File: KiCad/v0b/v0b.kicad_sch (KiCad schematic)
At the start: 34 parts, among them U1 SST39SF040, U10 MCP1700, U2 74HC139, U3 74HC174, U4 74HC191, U5 74HC191, U6 74HC191, U7 74HC670, U8 62256, U9 SAM2695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

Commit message: v0b update
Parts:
- removed R6: 3.3KΩ, PCM_Resistor_THT_AKL:R_Axial_DIN0204_L3.6mm_D1.6mm_P2.54mm_Vertical, symbol Device:R_Small
- removed RN1: R_Network03, Resistor_THT:R_Array_SIP4, symbol Device:R_Network03
- added C17: 1nF, Capacitor_THT:C_Disc_D3.0mm_W1.6mm_P2.50mm, symbol Device:C_Small
- added D1: 1N4148, Diode_THT:D_DO-34_SOD68_P2.54mm_Vertical_AnodeUp, symbol Diode:1N4148
- added R4: 4.7K, PCM_Resistor_THT_AKL:R_Axial_DIN0204_L3.6mm_D1.6mm_P2.54mm_Vertical, symbol Device:R_Small
- added RN1: R_Network04, Resistor_THT:R_Array_SIP5, symbol Device:R_Network04
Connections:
- net +3V3: no longer U9.38 (~{RST}/~{PD})
- net GND: now also R4.1
- net VCC: now also C17.2; no longer U3.1 (~{Mr})
- net pA11: now also RN1.1 (common)
- net pBank0: now also RN1.5 (R4)
- net pBank1: now also RN1.3 (R2)
- net pBank2: now also RN1.4 (R3)
- net pBank3: now also RN1.2 (R1)
- net at H1.32 (M2): now also D1.2 (A)
- new net ~{RESET}: C17.1, D1.1 (K), R4.2, U3.1 (~{Mr}), U9.38 (~{RST}/~{PD})
- no-connect marks 24 -> 23

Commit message: update v0b and README documentation
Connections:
- net cD4: no longer U3.14 (D5)
- net cD5: no longer U3.3 (D0)
- net cD6: now also U3.3 (D0)
- net cD7: now also U3.14 (D5)
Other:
- note added: ".... bbbb"
- note added: "dddd dddd"
- note added: "is.. bbbb"
- moved on the sheet: C1, C2, U10

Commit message: update v0b
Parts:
- added JP2, JP3, JP4: SolderJumper_2_Open, Jumper:SolderJumper-2_P1.3mm_Open_RoundedPad1.0x1.5mm, symbol Jumper:SolderJumper_2_Open
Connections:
- net pA11: now also JP2.1 (A)
- net pA12: now also JP3.1 (A)
- net pA13: now also JP4.1 (A)
- net pBank0: now also JP2.2 (B)
- net pBank1: now also JP3.2 (B)
- net pBank2: now also JP4.2 (B)
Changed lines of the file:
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@@
   (junction (at 81.28 124.46) (diameter 0) (color 0 0 0 0)
   )
+  (junction (at 72.39 80.645) (diameter 0) (color 0 0 0 0)
+  )
   (junction (at 68.58 190.5) (diameter 0) (color 0 0 0 0)
   )
@@
   (junction (at 21.59 163.83) (diameter 0) (color 0 0 0 0)
   )
+  (junction (at 69.85 76.2) (diameter 0) (color 0 0 0 0)
+  )
   (junction (at 246.38 157.48) (diameter 0) (color 0 0 0 0)
   )
@@
   )
   (junction (at 77.47 124.46) (diameter 0) (color 0 0 0 0)
+  )
+  (junction (at 74.93 85.09) (diameter 0) (color 0 0 0 0)
   )
   (junction (at 137.795 32.385) (diameter 0) (color 0 0 0 0)
@@
     (stroke (width 0) (type default))
   )
+  (wire (pts (xy 74.93 73.025) (xy 74.93 85.09))
+    (stroke (width 0) (type default))
+  )
   (wire (pts (xy 77.47 124.46) (xy 81.28 124.46))
     (stroke (width 0) (type default))
@@
     (stroke (width 0) (type default))
   )
+  (wire (pts (xy 72.39 80.645) (xy 72.39 87.63))
+    (stroke (width 0) (type default))
+  )
   (wire (pts (xy 117.475 59.055) (xy 111.125 59.055))
     (stroke (width 0) (type default))
@@
     (stroke (width 0) (type default))
   )
+  (wire (pts (xy 72.39 73.025) (xy 72.39 80.645))
+    (stroke (width 0) (type default))
+  )
   (wire (pts (xy 252.73 157.48) (xy 259.08 157.48))
     (stroke (width 0) (type default))
@@
     (stroke (width 0) (type default))
   )
+  (wire (pts (xy 69.85 76.2) (xy 69.85 87.63))
+    (stroke (width 0) (type default))
+  )
   (wire (pts (xy 68.58 190.5) (xy 71.12 190.5))
     (stroke (width 0) (type default))
   )
+  (wire (pts (xy 69.85 73.025) (xy 69.85 76.2))
+    (stroke (width 0) (type default))
+  )
   (wire (pts (xy 193.04 118.11) (xy 203.2 118.11))
     (stroke (width 0) (type default))
@@
   )
   (wire (pts (xy 31.75 162.56) (xy 31.75 163.83))
+    (stroke (width 0) (type default))
+  )
+  (wire (pts (xy 74.93 85.09) (xy 74.93 87.63))
     (stroke (width 0) (type default))
   )
@@
     (effects (font (size 1.27 1.27)) (justify right bottom))
   )
+  (label "pA12" (at 64.77 80.645 180) (fields_autoplaced)
+    (effects (font (size 1.27 1.27)) (justify right bottom))
+  )
   (label "cBank2" (at 36.83 87.63 90) (fields_autoplaced)
     (effects (font (size 1.27 1.27)) (justify left bottom))
@@
     (effects (font (size 1.27 1.27)) (justify left bottom))
   )
-  (label "pBank1" (at 72.39 87.63 90) (fields_autoplaced)
+  (label "pBank1" (at 72.39 73.025 90) (fields_autoplaced)
     (effects (font (size 1.27 1.27)) (justify left bottom))
   )
@@
     (effects (font (size 1.27 1.27)) (justify right bottom))
   )
+  (label "pA13" (at 67.31 85.09 180) (fields_autoplaced)
+    (effects (font (size 1.27 1.27)) (justify right bottom))
+  )
   (label "cD4" (at 137.795 118.745 180) (fields_autoplaced)
     (effects (font (size 1.27 1.27)) (justify right bottom))
@@
     (effects (font (size 1.27 1.27)) (justify right bottom))
   )
+  (label "pA11" (at 62.23 76.2 180) (fields_autoplaced)
+    (effects (font (size 1.27 1.27)) (justify right bottom))
+  )
   (label "cD0" (at 105.41 175.26 0) (fields_autoplaced)
     (effects (font (size 1.27 1.27)) (justify left bottom))
@@
     (effects (font (size 1.27 1.27)) (justify right bottom))
   )
-  (label "pBank0" (at 69.85 87.63 90) (fields_autoplaced)
+  (label "pBank0" (at 69.85 73.025 90) (fields_autoplaced)
     (effects (font (size 1.27 1.27)) (justify left bottom))
   )
@@
     (effects (font (size 1.27 1.27)) (justify right bottom))
   )
-  (label "pBank2" (at 74.93 87.63 90) (fields_autoplaced)
+  (label "pBank2" (at 74.93 73.025 90) (fields_autoplaced)
     (effects (font (size 1.27 1.27)) (justify left bottom))
   )
@@
     )
   )
+  (symbol (lib_id "Jumper:SolderJumper_2_Open") (at 71.12 85.09 0) (unit 1)
+    (in_bom yes) (on_board yes) (dnp no)
+    (property "Reference" "JP4" (at 71.12 78.74 0)
+      (effects (font (size 1.27 1.27)))
+    )
+    (property "Value" "SolderJumper_2_Open" (at 51.435 85.725 0)
+      (effects (font (size 1.27 1.27)))
+    )
+    (property "Footprint" "Jumper:SolderJumper-2_P1.3mm_Open_RoundedPad1.0x1.5mm" (at 71.12 85.09 0)
+      (effects (font (size 1.27 1.27)) hide)
+    )
+    (property "Datasheet" "~" (at 71.12 85.09 0)
+      (effects (font (size 1.27 1.27)) hide)
+    )
+    (pin "2")
+    (pin "1")
+    (instances
+      (project "v0b"
+        (path "/06c728bd-36f8-4444-b104-295b6423c2d2"
+          (reference "JP4") (unit 1)
+        )
+      )
+    )
+  )
   (symbol (lib_id "power:VCC") (at 62.23 100.33 180) (unit 1)
     (in_bom yes) (on_board yes) (dnp no)
@@
         (path "/06c728bd-36f8-4444-b104-295b6423c2d2"
           (reference "#PWR05") (unit 1)
+        )
+      )
+    )
+  )
+  (symbol (lib_id "Jumper:SolderJumper_2_Open") (at 66.04 76.2 0) (unit 1)
+    (in_bom yes) (on_board yes) (dnp no)
+    (property "Reference" "JP2" (at 66.04 69.85 0)
+      (effects (font (size 1.27 1.27)))
+    )
+    (property "Value" "SolderJumper_2_Open" (at 46.355 76.835 0)
+      (effects (font (size 1.27 1.27)))
+    )
+    (property "Footprint" "Jumper:SolderJumper-2_P1.3mm_Open_RoundedPad1.0x1.5mm" (at 66.04 76.2 0)
+      (effects (font (size 1.27 1.27)) hide)
+    )
+    (property "Datasheet" "~" (at 66.04 76.2 0)
+      (effects (font (size 1.27 1.27)) hide)
+    )
+    (pin "2")
+    (pin "1")
+    (instances
+      (project "v0b"
+        (path "/06c728bd-36f8-4444-b104-295b6423c2d2"
+          (reference "JP2") (unit 1)
         )
       )
@@
         )
       )
+    )
+  )
+  (symbol (lib_id "Jumper:SolderJumper_2_Open") (at 68.58 80.645 0) (unit 1)
+    (in_bom yes) (on_board yes) (dnp no)
+    (property "Reference" "JP3" (at 68.58 74.295 0)
+      (effects (font (size 1.27 1.27)))
+    )
+    (property "Value" "SolderJumper_2_Open" (at 48.895 81.28 0)
+      (effects (font (size 1.27 1.27)))
+    )
+    (property "Footprint" "Jumper:SolderJumper-2_P1.3mm_Open_RoundedPad1.0x1.5mm" (at 68.58 80.645 0)
+      (effects (font (size 1.27 1.27)) hide)
+    )
+    (property "Datasheet" "~" (at 68.58 80.645 0)
+      (effects (font (size 1.27 1.27)) hide)
+    )
+    (pin "2")
+    (pin "1")
+    (instances
+      (project "v0b"
+        (path "/06c728bd-36f8-4444-b104-295b6423c2d2"
+          (reference "JP3") (unit 1)
+        )
+      )

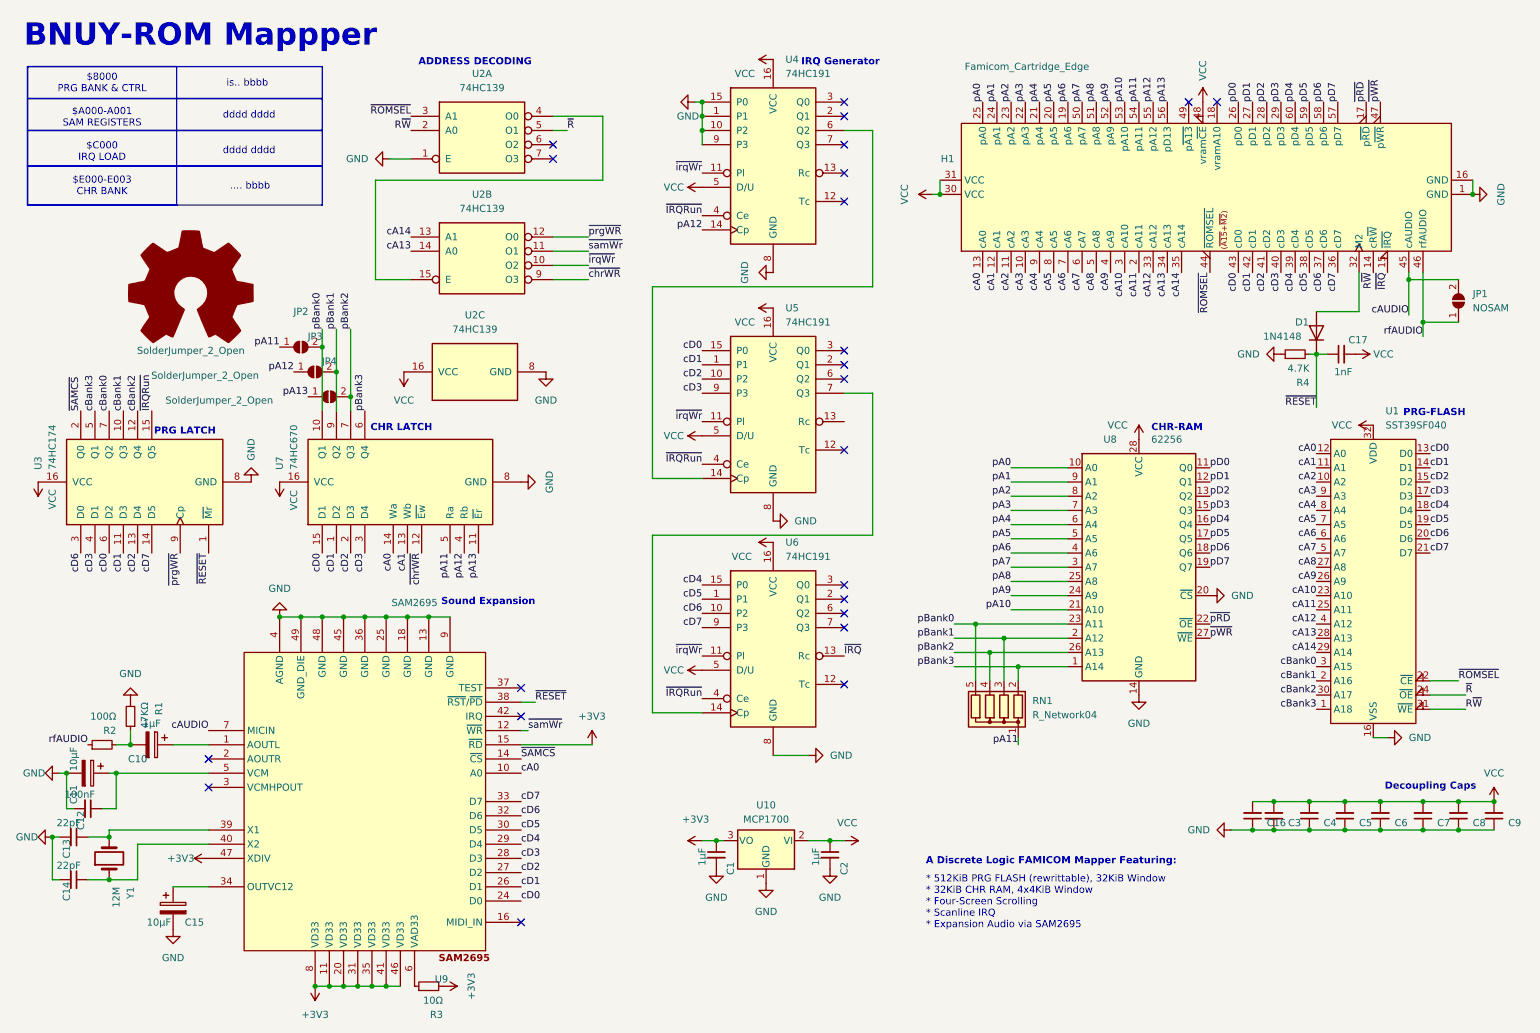
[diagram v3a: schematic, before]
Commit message: Update README, v0b schematic
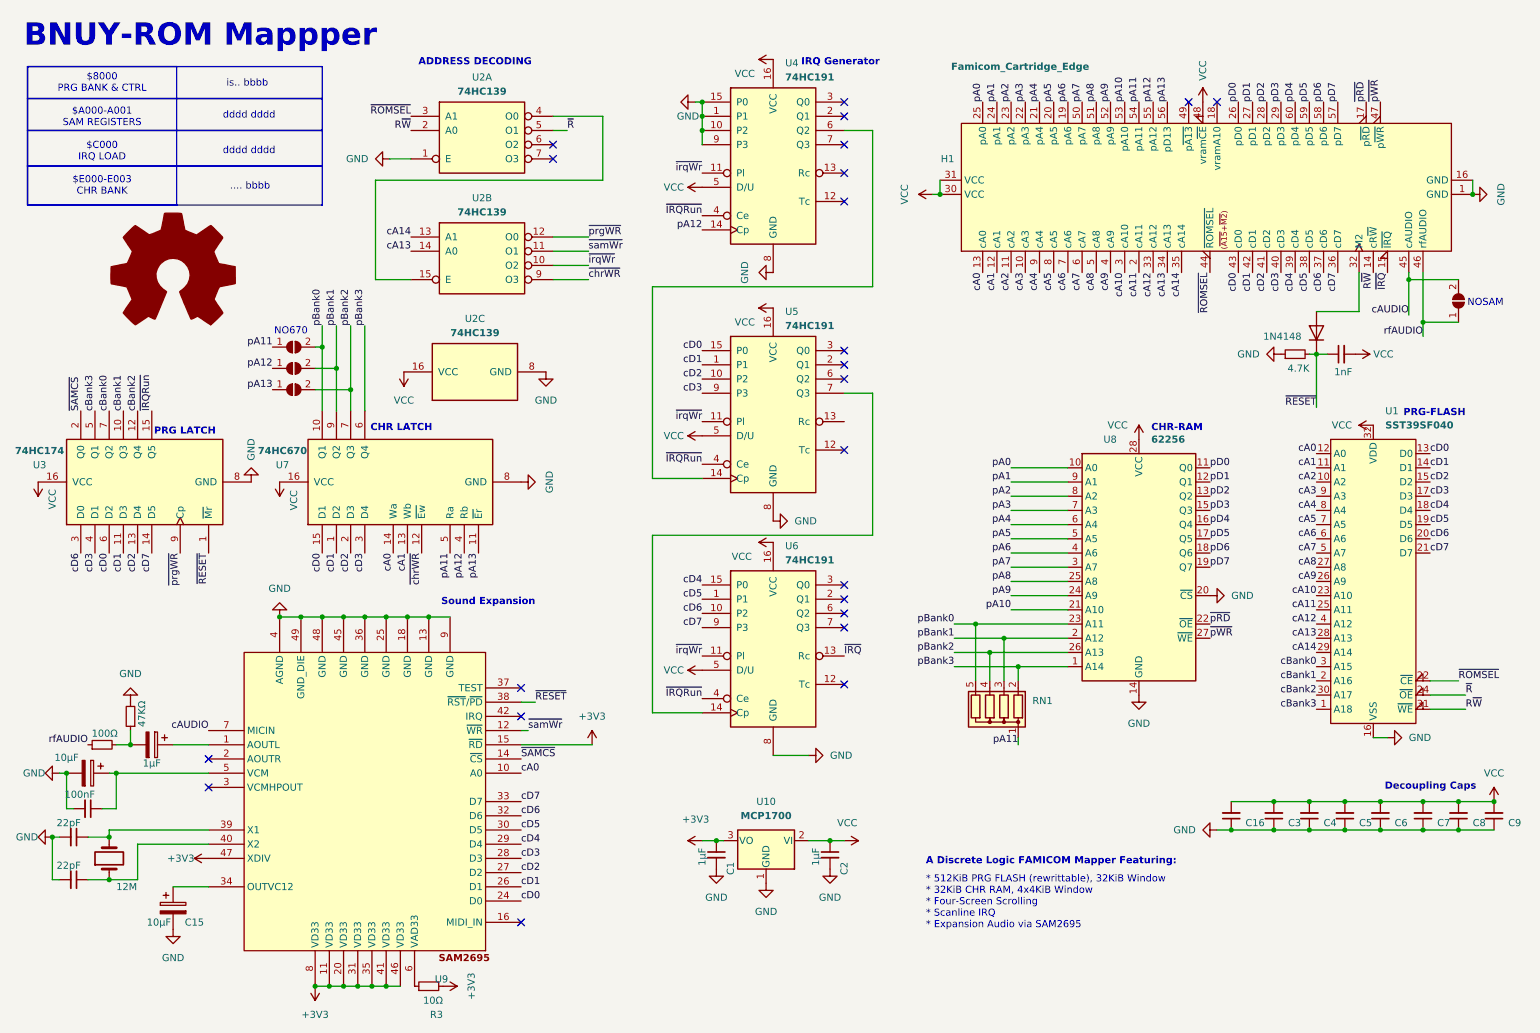
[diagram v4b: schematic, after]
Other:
- note added: "NO670"
- note added: "NOSAM"
- moved on the sheet: C16
